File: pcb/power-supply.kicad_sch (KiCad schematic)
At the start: 6 parts, among them IC1 AP2112K-3.3TRG1

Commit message: continued work on schematic
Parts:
- added C4, C6: 22u, SMT:0603, symbol generic:C
- added C5: 47p, SMT:0603, symbol generic:C
- added C7: 10u, SMT:0603, symbol generic:C
- added L1: 3u3, symbol generic:L
- added R10, R5, R8: 10k, SMT:0603, symbol generic:R
- added R11: 1k5, SMT:0603, symbol generic:R
- added R6: 22k, SMT:0603, symbol generic:R
- added R7: 750uR, SMT:0603, symbol generic:R
- added R9: 56k2, SMT:0603, symbol generic:R
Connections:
- net 3V3: now also R6.2
- net Battery: now also C7.1, R10.2, R7.1
- net GND: now also C4.1, C4.2, C5.1, C6.1, C6.2, C7.2, L1.2, R11.1, R5.1, R8.2, R9.1
- net +: now reaches R2.2
- net +: now also R7.2
- new net: R10.1, R11.2
- new net: R5.2, R6.1
- new net: C5.2, R8.1, R9.2
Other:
- note added: "-10 ... 30 A"
- note added: "18.3 V"
- note added: "UVLO R11 = 1.2V * 10k/(Uth - 1.2V) 2s: 6V = 2.5k -> 2k49 3s: 9V = 1.5k -> 1k5 4s: 12V = 1.1k -> 1k1 remove R11 if not needed"
- note removed: "3557-15"
- note removed: "XT-60 Male"
- moved on the sheet: C1, C2, C3, IC1, R1, R2

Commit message: schematic mostly done
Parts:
- removed R10: 10k, SMT:0603, symbol generic:R
- added C21, C22, C23: 100n, SMT:0603, symbol generic:C
- added IC3: INA199B2, symbol amplifiers:INA199B2
- added IC4: AP62300TWU-7, SOT:SOT-23-6, symbol Power:AP62300TWU-7
- added R10: 100k, symbol generic:Trimmer
- R11: value 1k5 -> 10k
- R2: value 150k -> 167k
- R5: value 10k -> 11k
- R7: footprint SMT:0603 -> (none)
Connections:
- net +: now also IC3.4 (IN+)
- net 3V3: now also IC3.3 (V+)
- net Battery: now also IC3.5 (IN-), IC4.1 (Vin), R10.3
- net GND: now also C22.2, C23.2, IC3.2 (GND), IC4.3 (GND), R10.1; no longer R11.1
- net I_bat: now also R11.1, C22.1
- net at R11.2: now also IC3.6 (OUT)
- net at R5.2, R6.1: now also IC3.1 (REF)
- net at C5.2, R8.1, R9.2: now also IC4.6 (FB)
- net at L1.1: now also C21.2, IC4.2 (SW)
- new net: C23.1, IC4.5 (EN), R10.2
- new net: C21.1, IC4.4 (BST)
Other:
- note added: "20V -> 3.3V"
- note removed: "18.3 V"
- note removed: "AP62300TWU-7"
- note removed: "INA199B2DCKR"
- note removed: "UVLO R11 = 1.2V * 10k/(Uth - 1.2V) 2s: 6V = 2.5k -> 2k49 3s: 9V = 1.5k -> 1k5 4s: 12V = 1.1k -> 1k1 remove R11 if not needed"
- title: (none) -> CAN bus to RC servo adapter
- moved on the sheet: C1, C2, C3, C4, C5, C6, C7, IC1, L1, R1, R2, R5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

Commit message: fixed 5V being GND net
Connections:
- net GND: no longer C1.1, C4.1, C5.1, C6.1, IC1.1 (VIN), IC1.3 (EN), L1.2, R8.2
- new net 5V: C1.1, C4.1, C5.1, C6.1, IC1.1 (VIN), IC1.3 (EN), L1.2, R8.2

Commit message: added DIP switches, footprints
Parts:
- IC3: footprint (none) -> sc70:SC70-6L
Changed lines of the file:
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@@
       (effects (font (size 1.27 1.27)) (justify left bottom))
     )
-    (property "Footprint" "" (at 86.36 101.6 0)
+    (property "Footprint" "sc70:SC70-6L" (at 86.36 101.6 0)
       (effects (font (size 1.27 1.27)) hide)
     )

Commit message: updated components. worked on layout
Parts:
- added C25: 100n, SMT:0603, symbol generic:C
- L1: footprint (none) -> inductor:5x5; DigiKey (none) -> 445-174398-1-ND; MPN (none) -> VLS5045EX-3R3N
- R7: footprint (none) -> SMT:2512-high-current
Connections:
- net 3V3: now also C25.1
- net GND: now also C25.2
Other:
- moved on the sheet: C22, IC3, R11, R5, R6

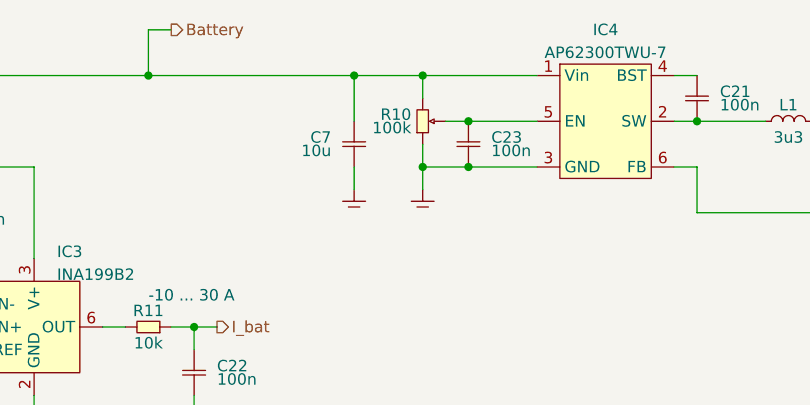
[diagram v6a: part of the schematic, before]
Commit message: added missing footprints
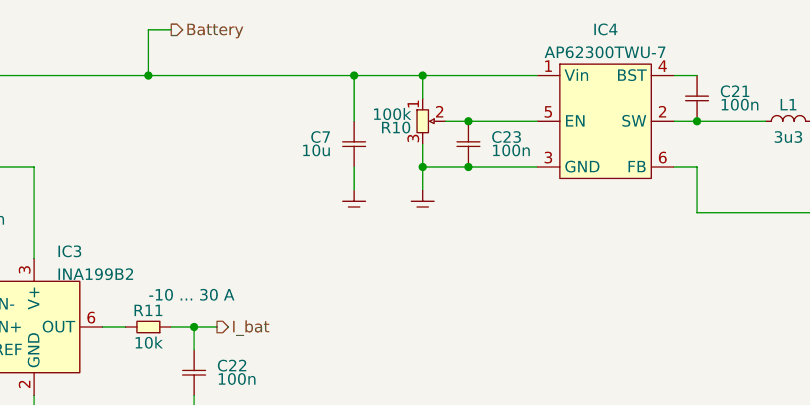
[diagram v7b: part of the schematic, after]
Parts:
- R10: footprint (none) -> potentiometers:3362P; symbol generic:Trimmer -> passives:3362P-1-104LF; DigiKey (none) -> 3362P-104LF-ND; MPN (none) -> 3362P-1-104LF
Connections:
- net Battery: now also R10.1; no longer R10.3
- net GND: now also R10.3; no longer R10.1
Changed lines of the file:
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@@
     )
   )
-  (symbol (lib_id "generic:Trimmer") (at 132.08 99.06 90) (unit 1)
+  (symbol (lib_id "passives:3362P-1-104LF") (at 132.08 99.06 90) (mirror x) (unit 1)
     (in_bom yes) (on_board yes) (dnp no)
     (property "Reference" "R10" (at 130.81 99.06 90)
@@
       (effects (font (size 1.27 1.27)) (justify left bottom))
     )
-    (property "Footprint" "" (at 127 91.44 0)
+    (property "Footprint" "potentiometers:3362P" (at 124.46 93.98 0)
       (effects (font (size 1.27 1.27)) hide)
     )
-    (property "Datasheet" "" (at 132.08 99.06 0)
+    (property "Datasheet" "https://www.bourns.com/docs/Product-Datasheets/3362.pdf" (at 132.08 99.06 0)
       (effects (font (size 1.27 1.27)) hide)
     )
+    (property "MPN" "3362P-1-104LF" (at 132.08 99.06 0)
+      (effects (font (size 1.27 1.27)) hide)
+    )
+    (property "DigiKey" "3362P-104LF-ND" (at 132.08 99.06 0)
+      (effects (font (size 1.27 1.27)) hide)
+    )

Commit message: worked on layout
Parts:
- added C8: 100n, SMT:0603, symbol generic:C
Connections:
- net GND: now also C8.2
- net at IC3.1 (REF), R5.2, R6.1: now also C8.1
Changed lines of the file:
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@@
   (junction (at 223.52 99.06) (diameter 0) (color 0 0 0 0)
   )
+  (junction (at 66.04 124.46) (diameter 0) (color 0 0 0 0)
+  )
   (junction (at 137.16 104.14) (diameter 0) (color 0 0 0 0)
   )
@@
     (stroke (width 0) (type default))
   )
+  (wire (pts (xy 66.04 124.46) (xy 81.28 124.46))
+    (stroke (width 0) (type default))
+  )
   (wire (pts (xy 33.02 104.14) (xy 33.02 106.68))
     (stroke (width 0) (type default))
@@
     (stroke (width 0) (type default))
   )
+  (wire (pts (xy 66.04 124.46) (xy 66.04 127))
+    (stroke (width 0) (type default))
+  )
   (wire (pts (xy 162.56 99.06) (xy 170.18 99.06))
     (stroke (width 0) (type default))
@@
     (stroke (width 0) (type default))
   )
-  (wire (pts (xy 58.42 124.46) (xy 81.28 124.46))
+  (wire (pts (xy 58.42 124.46) (xy 66.04 124.46))
     (stroke (width 0) (type default))
   )
@@
   )
   (wire (pts (xy 177.8 99.06) (xy 177.8 101.6))
+    (stroke (width 0) (type default))
+  )
+  (wire (pts (xy 66.04 132.08) (xy 66.04 134.62))
     (stroke (width 0) (type default))
   )
@@
         (path "/6bb3bad6-1a89-4624-b34d-6ddda7dd16d2/bd5ce3a2-965f-4825-a529-9d15232fee93"
           (reference "#GND027") (unit 1)
+        )
+      )
+    )
+  )
+  (symbol (lib_id "generic:GND") (at 66.04 134.62 0) (unit 1)
+    (in_bom yes) (on_board yes) (dnp no) (fields_autoplaced)
+    (property "Reference" "#GND035" (at 69.85 133.35 0)
+      (effects (font (size 1.27 1.27)) hide)
+    )
+    (property "Value" "GND" (at 69.85 134.62 0)
+      (effects (font (size 1.27 1.27)) hide)
+    )
+    (property "Footprint" "" (at 66.04 134.62 0)
+      (effects (font (size 1.27 1.27)) hide)
+    )
+    (property "Datasheet" "" (at 66.04 134.62 0)
+      (effects (font (size 1.27 1.27)) hide)
+    )
+    (pin "~")
+    (instances
+      (project "pcb"
+        (path "/6bb3bad6-1a89-4624-b34d-6ddda7dd16d2/bd5ce3a2-965f-4825-a529-9d15232fee93"
+          (reference "#GND035") (unit 1)
         )
       )
@@
         )
       )
+    )
+  )
+  (symbol (lib_id "generic:C") (at 66.04 129.54 0) (unit 1)
+    (in_bom yes) (on_board yes) (dnp no)
+    (property "Reference" "C8" (at 68.58 129.54 0)
+      (effects (font (size 1.27 1.27)) (justify left bottom))
+    )
+    (property "Value" "100n" (at 68.58 129.54 0)
+      (effects (font (size 1.27 1.27)) (justify left top))
+    )
+    (property "Footprint" "SMT:0603" (at 66.04 132.08 0)
+      (effects (font (size 1.27 1.27)) hide)
+    )
+    (property "Datasheet" "" (at 66.04 129.54 0)
+      (effects (font (size 1.27 1.27)) hide)
+    )
+    (pin "1")
+    (pin "2")
+    (instances
+      (project "pcb"
+        (path "/6bb3bad6-1a89-4624-b34d-6ddda7dd16d2/bd5ce3a2-965f-4825-a529-9d15232fee93"
+          (reference "C8") (unit 1)
+        )
+      )
